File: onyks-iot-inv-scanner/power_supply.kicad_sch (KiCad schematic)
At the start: 47 parts, among them IC1 TPS22953DSQR, IC2 TPS22953DSQR, IC3 SN74LVC1G06DBVT, IC5 TPS63021DSJR, Q1 DMN3150L, Q2 DMN3150L, U1 DW01A, U3 TP4056-42-ESOP8, U4 TPS62A02ADRL, U5 TPS62A02ADRL

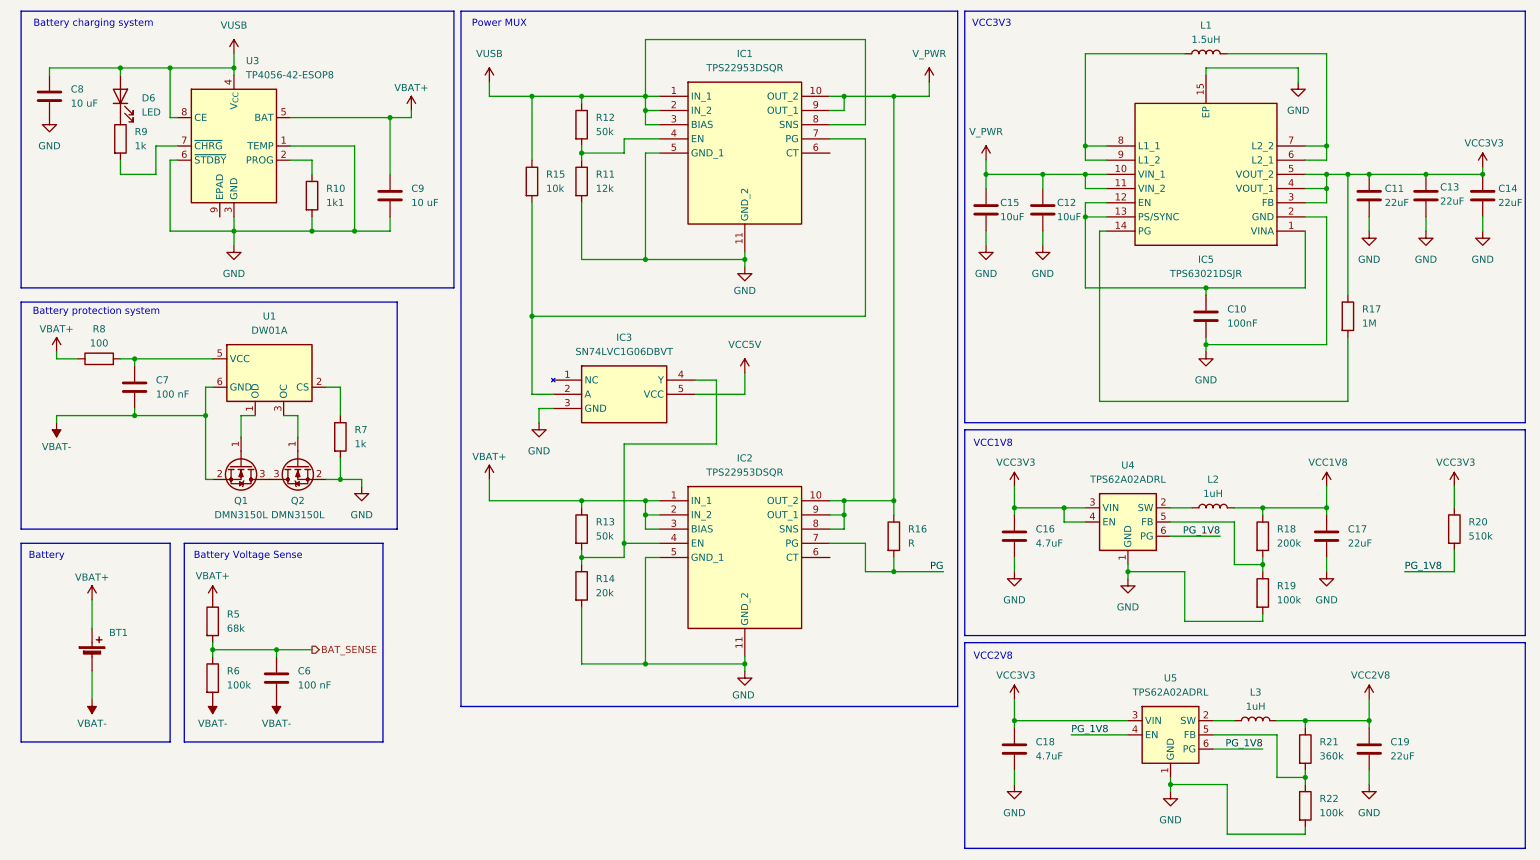
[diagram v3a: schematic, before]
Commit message: net labels correction and connected batsense
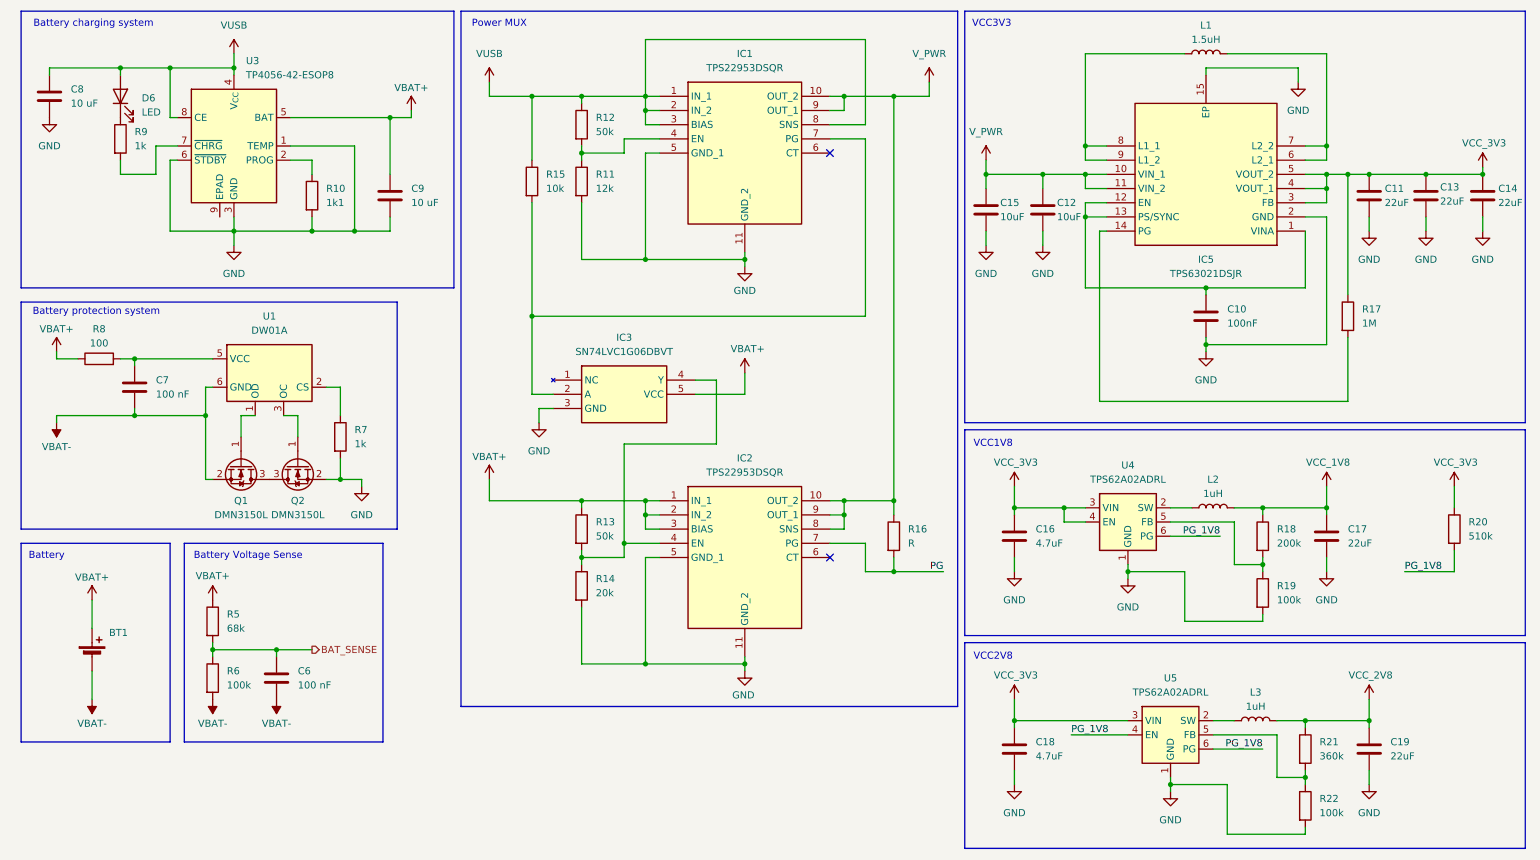
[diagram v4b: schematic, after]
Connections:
- net VCC5V is gone; now on net VBAT+: IC3.5 (VCC)
- net VCC1V8 renamed VCC_1V8
- net VCC2V8 renamed VCC_2V8
- net VCC3V3 renamed VCC_3V3
- no-connect marks 0 -> 2
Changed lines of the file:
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@@
 		(color 0 0 0 0)
 	)
+	(no_connect
+		(at 158.75 111.76)
+	)
+	(no_connect
+		(at 158.75 39.37)
+	)
 	(wire
 		(pts
@@
 			)
 		)
-		(property "Value" "VCC3V3"
+		(property "Value" "VCC_3V3"
 			(at 192.024 94.742 0)
 			(effects
@@
 		(on_board yes)
 		(dnp no)
-		(fields_autoplaced yes)
 		(property "Reference" "#PWR031"
 			(at 143.51 82.55 0)
@@
 			)
 		)
-		(property "Value" "VCC5V"
-			(at 143.51 73.66 0)
+		(property "Value" "VBAT+"
+			(at 140.97 74.422 0)
 			(effects
 				(font
 					(size 1.27 1.27)
 				)
+				(justify left)
 			)
 		)
@@
 			)
 		)
-		(property "Value" "VCC2V8"
+		(property "Value" "VCC_2V8"
 			(at 255.524 132.842 0)
 			(effects
@@
 			)
 		)
-		(property "Value" "VCC3V3"
+		(property "Value" "VCC_3V3"
 			(at 275.844 37.592 0)
 			(effects
@@
 			)
 		)
-		(property "Value" "VCC3V3"
+		(property "Value" "VCC_3V3"
 			(at 270.764 94.742 0)
 			(effects
@@
 			)
 		)
-		(property "Value" "VCC1V8"
+		(property "Value" "VCC_1V8"
 			(at 247.904 94.742 0)
 			(effects
@@
 			)
 		)
-		(property "Value" "VCC3V3"
+		(property "Value" "VCC_3V3"
 			(at 192.024 132.842 0)
 			(effects

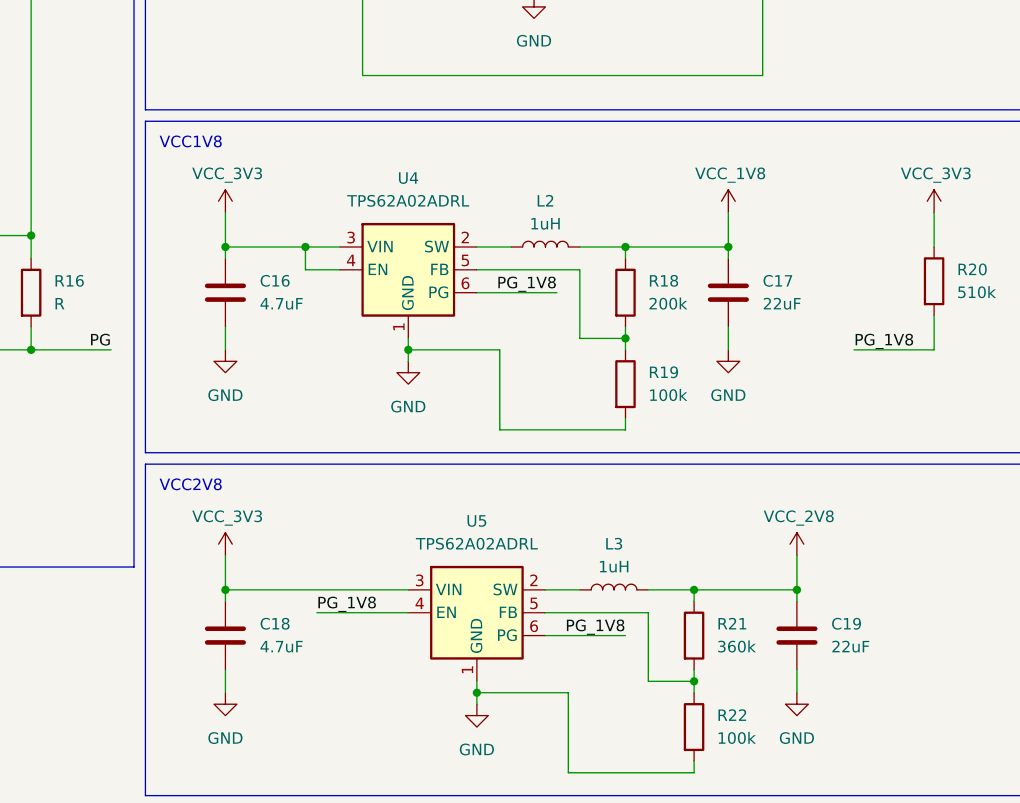
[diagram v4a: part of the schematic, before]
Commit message: moved camera to separate schematic and added llc's for it
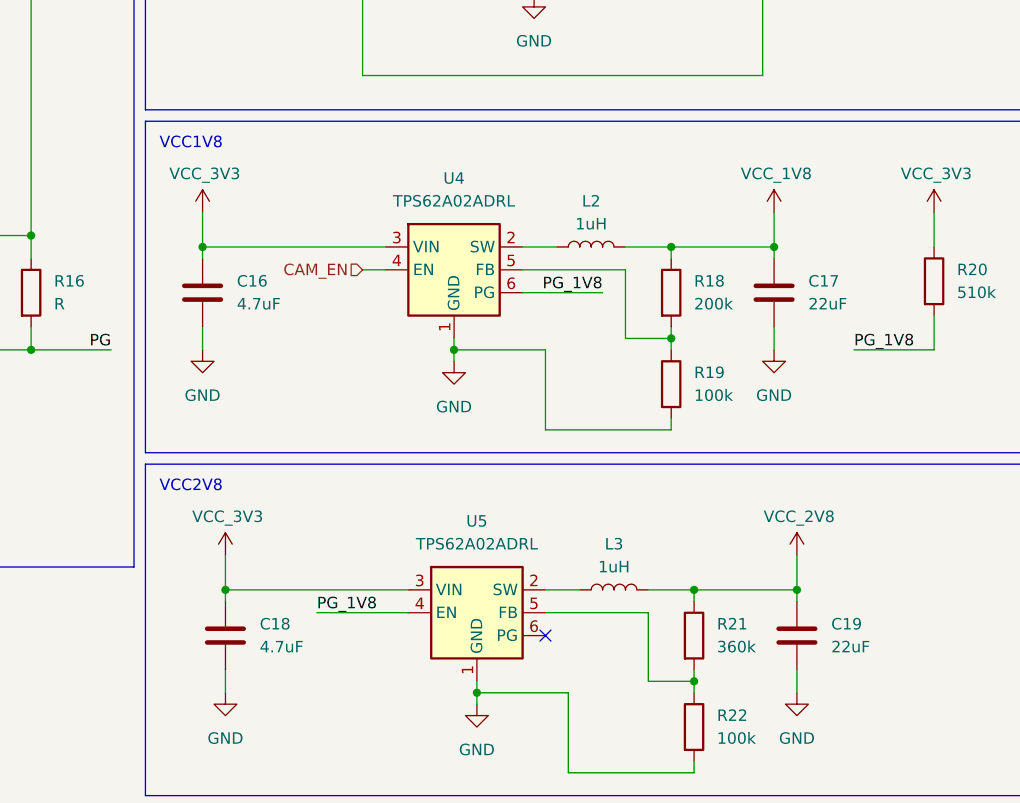
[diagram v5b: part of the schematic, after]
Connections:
- net PG_1V8: no longer U5.6 (PG)
- net VCC_3V3: no longer U4.4 (EN)
- new net CAM_EN: U4.4 (EN)
- no-connect marks 2 -> 3
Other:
- moved on the sheet: C16, C17, L2, R18, R19, U4
